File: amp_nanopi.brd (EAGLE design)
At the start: 87.1 x 64 mm, 11 parts, among them J1 MF-CON-2.54mm-01x02, J2 MF-CON-2.54mm-01x02, J3 MF-CON-2.54mm-01x02, X2 B3P-VH-2, X3 B3P-VH-2

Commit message: dostosowanie do nowego projektu safe_pi_shutdown
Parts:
- removed SV1: (no value), con-lstb:MA12-2
- added X1: B3P-VH-2, jst-vh:B3P-VH-2
- X3: value B3P-VH-2 -> (none); device jst-vh:B3P-VH-2 -> con-lstb:MA12-2
- moved X3 53.2 mm to (66.4, 5.00), flipped to the bottom, turned to 180 degrees
- renumbered SV2 to X4, U$1 to U1
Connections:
- net GND: now also X3.14, X3.20, X3.6, X3.9; no longer SV1.14, SV1.20, SV1.6, SV1.9
- net N$4: now also X1.1; no longer X3.1
- net N$6: now also X1.3; no longer X3.3
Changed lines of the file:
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@@
 <attribute name="OC_FARNELL" value="959704" x="158.57" y="70.98" size="1.778" layer="27" rot="R90" display="off"/>
 </element>
-<element name="U$1" library="meanwell_irm_v5" package="IRM_05/10" value="" x="32.7" y="23.43" rot="R270"/>
+<element name="U1" library="meanwell_irm_v5" package="IRM_05/10" value="" x="32.7" y="23.43" smashed="yes" rot="R270">
+<attribute name="NAME" x="33.97" y="25.97" size="1.27" layer="25" rot="R270"/>
+<attribute name="VALUE" x="30.16" y="25.97" size="1.27" layer="27" rot="R270"/>
+</element>
 <element name="F1" library="fuse" package="SH22,5" value="FUSESH22,5" x="14.38" y="39.17" smashed="yes" rot="R270">
 <attribute name="OC_NEWARK" value="unknown" x="-19.91" y="-4.01" size="1.778" layer="27" rot="R270" display="off"/>
@@
 <attribute name="MF" value="" x="-19.91" y="-4.01" size="1.778" layer="27" rot="R270" display="off"/>
 <attribute name="OC_FARNELL" value="unknown" x="-19.91" y="-4.01" size="1.778" layer="27" rot="R270" display="off"/>
-<attribute name="NAME" x="10.484" y="54.77" size="1.778" layer="25" ratio="10" rot="R270"/>
+<attribute name="NAME" x="13.984" y="55.27" size="1.778" layer="25" ratio="10" rot="R270"/>
 <attribute name="VALUE" x="19.184" y="54.127" size="1.778" layer="27" ratio="10" rot="R270"/>
 </element>
-<element name="F2" library="fuse" package="SH22,5" value="FUSESH22,5" x="5.12" y="39.27" rot="R90">
+<element name="F2" library="fuse" package="SH22,5" value="FUSESH22,5" x="5.12" y="39.27" smashed="yes" rot="R90">
 <attribute name="OC_NEWARK" value="unknown" x="52.11" y="69.75" size="1.778" layer="27" rot="R90" display="off"/>
 <attribute name="MPN" value="" x="52.11" y="69.75" size="1.778" layer="27" rot="R90" display="off"/>
 <attribute name="MF" value="" x="52.11" y="69.75" size="1.778" layer="27" rot="R90" display="off"/>
 <attribute name="OC_FARNELL" value="unknown" x="52.11" y="69.75" size="1.778" layer="27" rot="R90" display="off"/>
-</element>
-<element name="X2" library="jst-vh" package="B3P-VH-2" value="B3P-VH-2" x="29" y="56.4" rot="R270"/>
-<element name="X3" library="jst-vh" package="B3P-VH-2" value="B3P-VH-2" x="14.8" y="18.1" rot="R270"/>
-<element name="SV1" library="con-lstb" package="MA12-2" value="" x="66.4" y="5" rot="MR180">
+<attribute name="NAME" x="3.216" y="23.07" size="1.778" layer="25" ratio="10" rot="R90"/>
+<attribute name="VALUE" x="11.216" y="40.413" size="1.778" layer="27" ratio="10" rot="R90"/>
+</element>
+<element name="X2" library="jst-vh" package="B3P-VH-2" value="B3P-VH-2" x="29" y="56.4" smashed="yes" rot="R270">
+<attribute name="NAME" x="33.5" y="61.4" size="1.27" layer="25" ratio="10" rot="R270"/>
+<attribute name="VALUE" x="22" y="61.4" size="1.27" layer="27" rot="R270"/>
+</element>
+<element name="X1" library="jst-vh" package="B3P-VH-2" value="B3P-VH-2" x="14.8" y="18.1" smashed="yes" rot="R270">
+<attribute name="NAME" x="10.2" y="11.5" size="1.27" layer="25" ratio="10" rot="R270"/>
+<attribute name="VALUE" x="7.8" y="23.1" size="1.27" layer="27" rot="R270"/>
+</element>
+<element name="X3" library="con-lstb" package="MA12-2" value="" x="66.4" y="5" rot="MR180">
 <attribute name="OC_NEWARK" value="unknown" x="66.4" y="5" size="1.778" layer="28" rot="MR180" display="off"/>
 <attribute name="MPN" value="" x="66.4" y="5" size="1.778" layer="28" rot="MR180" display="off"/>
@@
 <attribute name="OC_FARNELL" value="unknown" x="66.4" y="5" size="1.778" layer="28" rot="MR180" display="off"/>
 </element>
-<element name="SV2" library="con-lstb" package="MA12-1" value="" x="66.4" y="41.2" rot="MR180">
+<element name="X4" library="con-lstb" package="MA12-1" value="" x="66.4" y="41.2" rot="MR180">
 <attribute name="OC_NEWARK" value="unknown" x="66.4" y="41.2" size="1.778" layer="28" rot="MR180" display="off"/>
 <attribute name="MPN" value="" x="66.4" y="41.2" size="1.778" layer="28" rot="MR180" display="off"/>
@@
 <signals>
 <signal name="VCC">
-<contactref element="U$1" pad="V+"/>
+<contactref element="U1" pad="V+"/>
 <contactref element="J2" pad="P$1"/>
 <wire x1="31.45" y1="4.18" x2="32.735" y2="4.18" width="1.27" layer="16"/>
@@
 </signal>
 <signal name="GND">
-<contactref element="U$1" pad="V-"/>
-<contactref element="SV1" pad="6"/>
-<contactref element="SV1" pad="14"/>
-<contactref element="SV1" pad="20"/>
-<contactref element="SV1" pad="9"/>
-<contactref element="SV2" pad="12"/>
+<contactref element="U1" pad="V-"/>
+<contactref element="X3" pad="6"/>
+<contactref element="X3" pad="14"/>
+<contactref element="X3" pad="20"/>
+<contactref element="X3" pad="9"/>
+<contactref element="X4" pad="12"/>
 <contactref element="S1" pad="1"/>
 <wire x1="23.5" y1="4.2" x2="23.45" y2="4.18" width="1.27" layer="16"/>
@@
 <contactref element="F1" pad="2"/>
 <contactref element="F2" pad="1"/>
-<contactref element="X3" pad="1"/>
+<contactref element="X1" pad="1"/>
 <wire x1="14.4" y1="22.5" x2="14.4" y2="27.9" width="2.032" layer="16"/>
 <wire x1="14.8" y1="22.1" x2="14.4" y2="22.5" width="2.032" layer="16"/>
@@
 <signal name="N$5" class="1">
 <contactref element="F1" pad="1"/>
-<contactref element="U$1" pad="AC/L"/>
+<contactref element="U1" pad="AC/L"/>
 <wire x1="22.1" y1="42.7" x2="23.4" y2="42.7" width="2.032" layer="16"/>
 <wire x1="14.4" y1="50.4" x2="22.1" y2="42.7" width="2.032" layer="16"/>
@@
 </signal>
 <signal name="N$6" class="1">
-<contactref element="U$1" pad="AC/N"/>
+<contactref element="U1" pad="AC/N"/>
 <contactref element="X2" pad="3"/>
-<contactref element="X3" pad="3"/>
+<contactref element="X1" pad="3"/>
 <wire x1="33.8" y1="47.6" x2="29" y2="52.4" width="2.032" layer="16"/>
 <wire x1="33.8" y1="43.6" x2="33.8" y2="47.6" width="2.032" layer="16"/>
@@
 </signal>
 <signal name="N$1">
-<contactref element="SV2" pad="7"/>
+<contactref element="X4" pad="7"/>
 <wire x1="67.7" y1="42.9" x2="67.7" y2="41.2" width="0.762" layer="16"/>
 <wire x1="69.7" y1="44.9" x2="67.7" y2="42.9" width="0.762" layer="16"/>

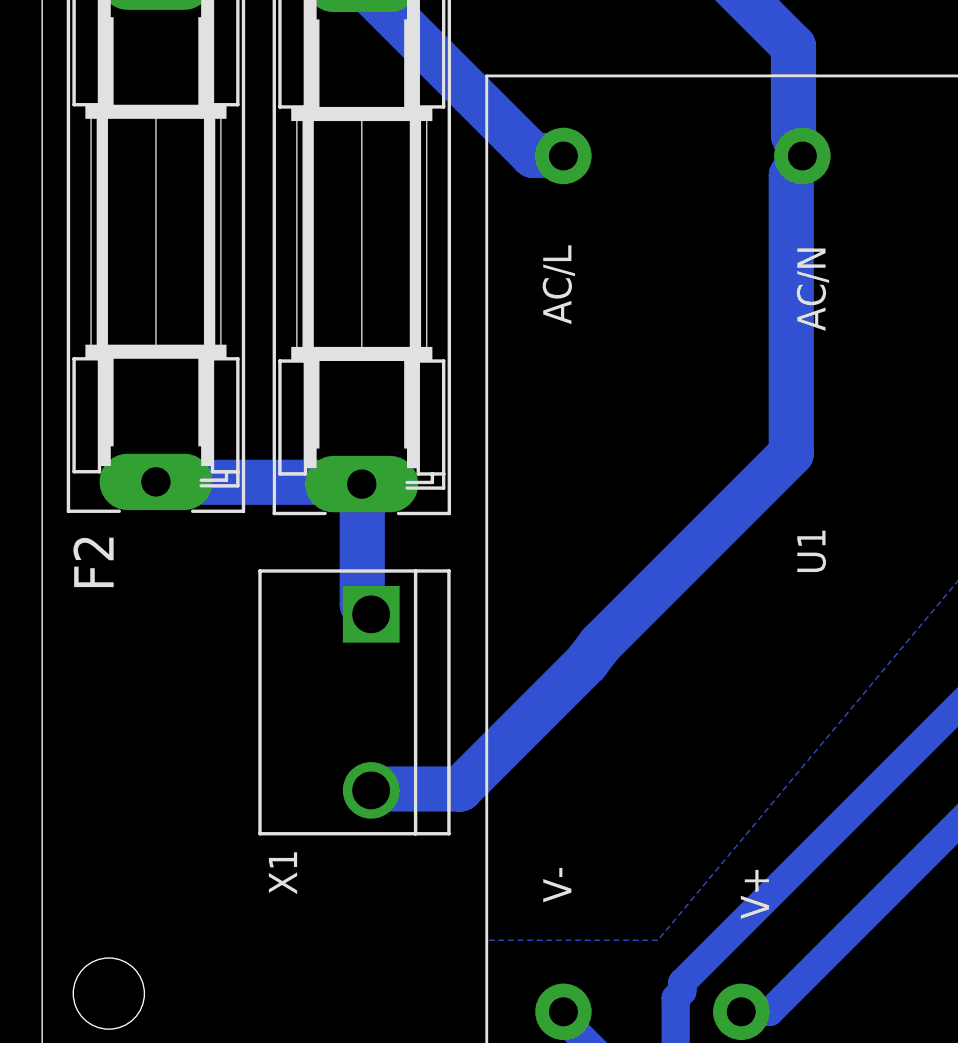
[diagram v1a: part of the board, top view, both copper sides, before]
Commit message: poprawka zlacza zasilania tak aby nie kolidowalo z zasilaczem
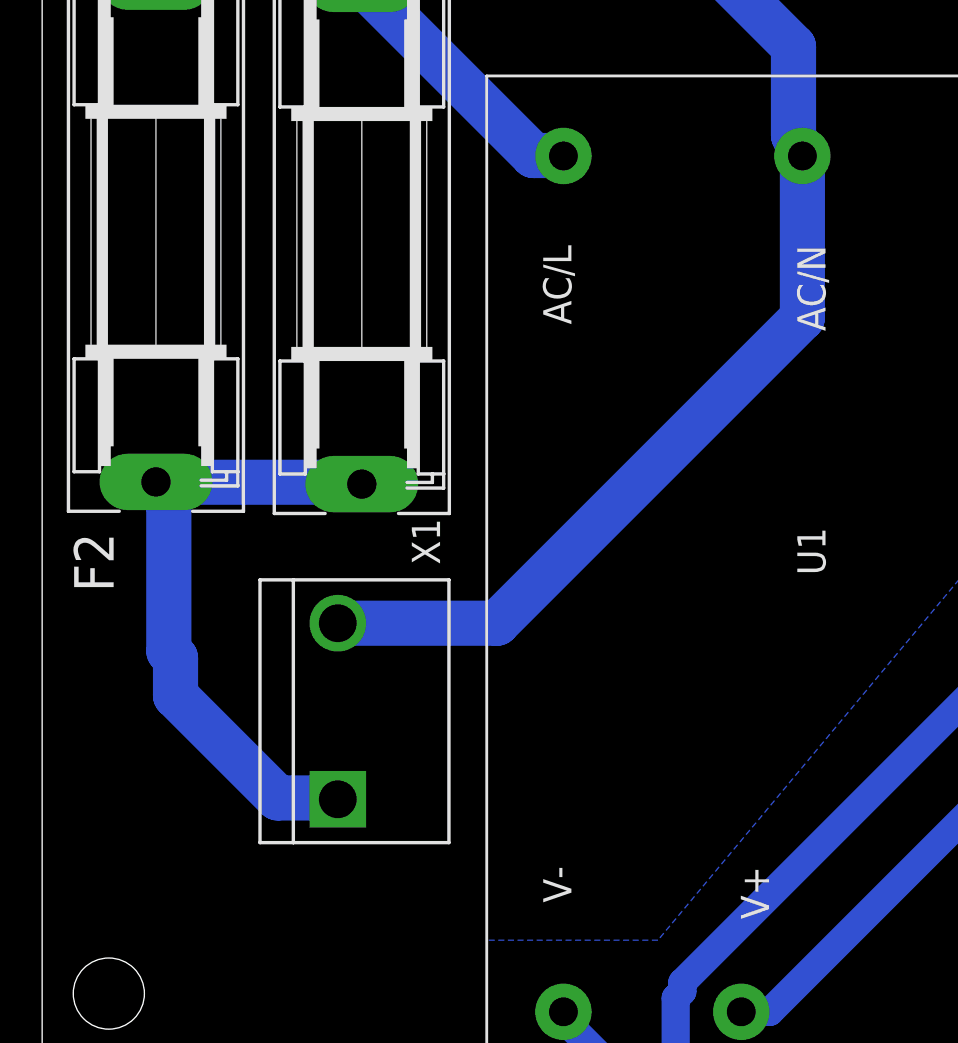
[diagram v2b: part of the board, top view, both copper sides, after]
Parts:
- moved X1 1.55 mm to (13.3, 17.7), turned to 90 degrees
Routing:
- net N$4: track 15.3 -> 28.4 mm
- net N$6: track 50.6 -> 45.7 mm
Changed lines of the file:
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@@
 <?xml version="1.0" encoding="utf-8"?>
 <!DOCTYPE eagle SYSTEM "eagle.dtd">
-<eagle version="6.6.0">
+<eagle version="6.5.0">
 <drawing>
 <settings>
@@
 <attribute name="VALUE" x="22" y="61.4" size="1.27" layer="27" rot="R270"/>
 </element>
-<element name="X1" library="jst-vh" package="B3P-VH-2" value="B3P-VH-2" x="14.8" y="18.1" smashed="yes" rot="R270">
-<attribute name="NAME" x="10.2" y="11.5" size="1.27" layer="25" ratio="10" rot="R270"/>
-<attribute name="VALUE" x="7.8" y="23.1" size="1.27" layer="27" rot="R270"/>
+<element name="X1" library="jst-vh" package="B3P-VH-2" value="B3P-VH-2" x="13.3" y="17.7" smashed="yes" rot="R90">
+<attribute name="NAME" x="17.9" y="24.3" size="1.27" layer="25" ratio="10" rot="R90"/>
+<attribute name="VALUE" x="20.3" y="12.7" size="1.27" layer="27" rot="R90"/>
 </element>
 <element name="X3" library="con-lstb" package="MA12-2" value="" x="66.4" y="5" rot="MR180">
@@
 <contactref element="F2" pad="1"/>
 <contactref element="X1" pad="1"/>
-<wire x1="14.4" y1="22.5" x2="14.4" y2="27.9" width="2.032" layer="16"/>
-<wire x1="14.8" y1="22.1" x2="14.4" y2="22.5" width="2.032" layer="16"/>
-<wire x1="14.4" y1="27.9" x2="14.38" y2="27.9178" width="2.032" layer="16"/>
-<wire x1="14.8" y1="22.1" x2="14.8" y2="22.06" width="2.032" layer="16"/>
 <wire x1="13.4" y1="28" x2="5.2" y2="28" width="2.032" layer="16"/>
 <wire x1="5.2" y1="28" x2="5.12" y2="28.0178" width="2.032" layer="16"/>
 <wire x1="13.4" y1="28" x2="14.38" y2="27.9178" width="2.032" layer="16"/>
+<wire x1="5.7" y1="20.4" x2="5.7" y2="27" width="2.032" layer="16"/>
+<wire x1="6" y1="20.1" x2="5.7" y2="20.4" width="2.032" layer="16"/>
+<wire x1="6" y1="18.4" x2="6" y2="20.1" width="2.032" layer="16"/>
+<wire x1="10.6" y1="13.8" x2="6" y2="18.4" width="2.032" layer="16"/>
+<wire x1="13.3" y1="13.8" x2="10.6" y2="13.8" width="2.032" layer="16"/>
+<wire x1="5.7" y1="27" x2="5.12" y2="28.0178" width="2.032" layer="16"/>
+<wire x1="13.3" y1="13.8" x2="13.3" y2="13.74" width="2.032" layer="16"/>
 </signal>
 <signal name="N$5" class="1">
@@
 <wire x1="29" y1="52.4" x2="29" y2="52.44" width="2.032" layer="16"/>
 <wire x1="33.8" y1="43.6" x2="34.2" y2="42.68" width="2.032" layer="16"/>
-<wire x1="18.8" y1="14.2" x2="24.5" y2="19.9" width="2.032" layer="16"/>
-<wire x1="14.8" y1="14.2" x2="18.8" y2="14.2" width="2.032" layer="16"/>
-<wire x1="14.8" y1="14.2" x2="14.8" y2="14.14" width="2.032" layer="16"/>
-<wire x1="33.7" y1="29.3" x2="33.7" y2="41.8" width="2.032" layer="16"/>
-<wire x1="25.1" y1="20.7" x2="33.7" y2="29.3" width="2.032" layer="16"/>
-<wire x1="33.7" y1="41.8" x2="34.2" y2="42.68" width="2.032" layer="16"/>
-<wire x1="25.1" y1="20.7" x2="24.5" y2="19.9" width="2.032" layer="16"/>
+<wire x1="13.3" y1="21.66" x2="20.46" y2="21.66" width="2.032" layer="16"/>
+<wire x1="20.46" y1="21.66" x2="34.2" y2="35.4" width="2.032" layer="16"/>
+<wire x1="34.2" y1="35.4" x2="34.2" y2="42.68" width="2.032" layer="16"/>
 </signal>
 <signal name="N$2" class="1">
